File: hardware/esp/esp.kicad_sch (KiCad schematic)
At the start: 41 parts, among them J1 Conn_01x02, J2 USB_C_Receptacle_USB2.0_16P, J3 USB_C_Receptacle_USB2.0_16P, J4 Conn_01x02, SW1 RESET, SW2 BOOT, U1 AMS1117-3.3, U2 CP2102N-Axx-xQFN20, U3 ESP32-S3-WROOM-1

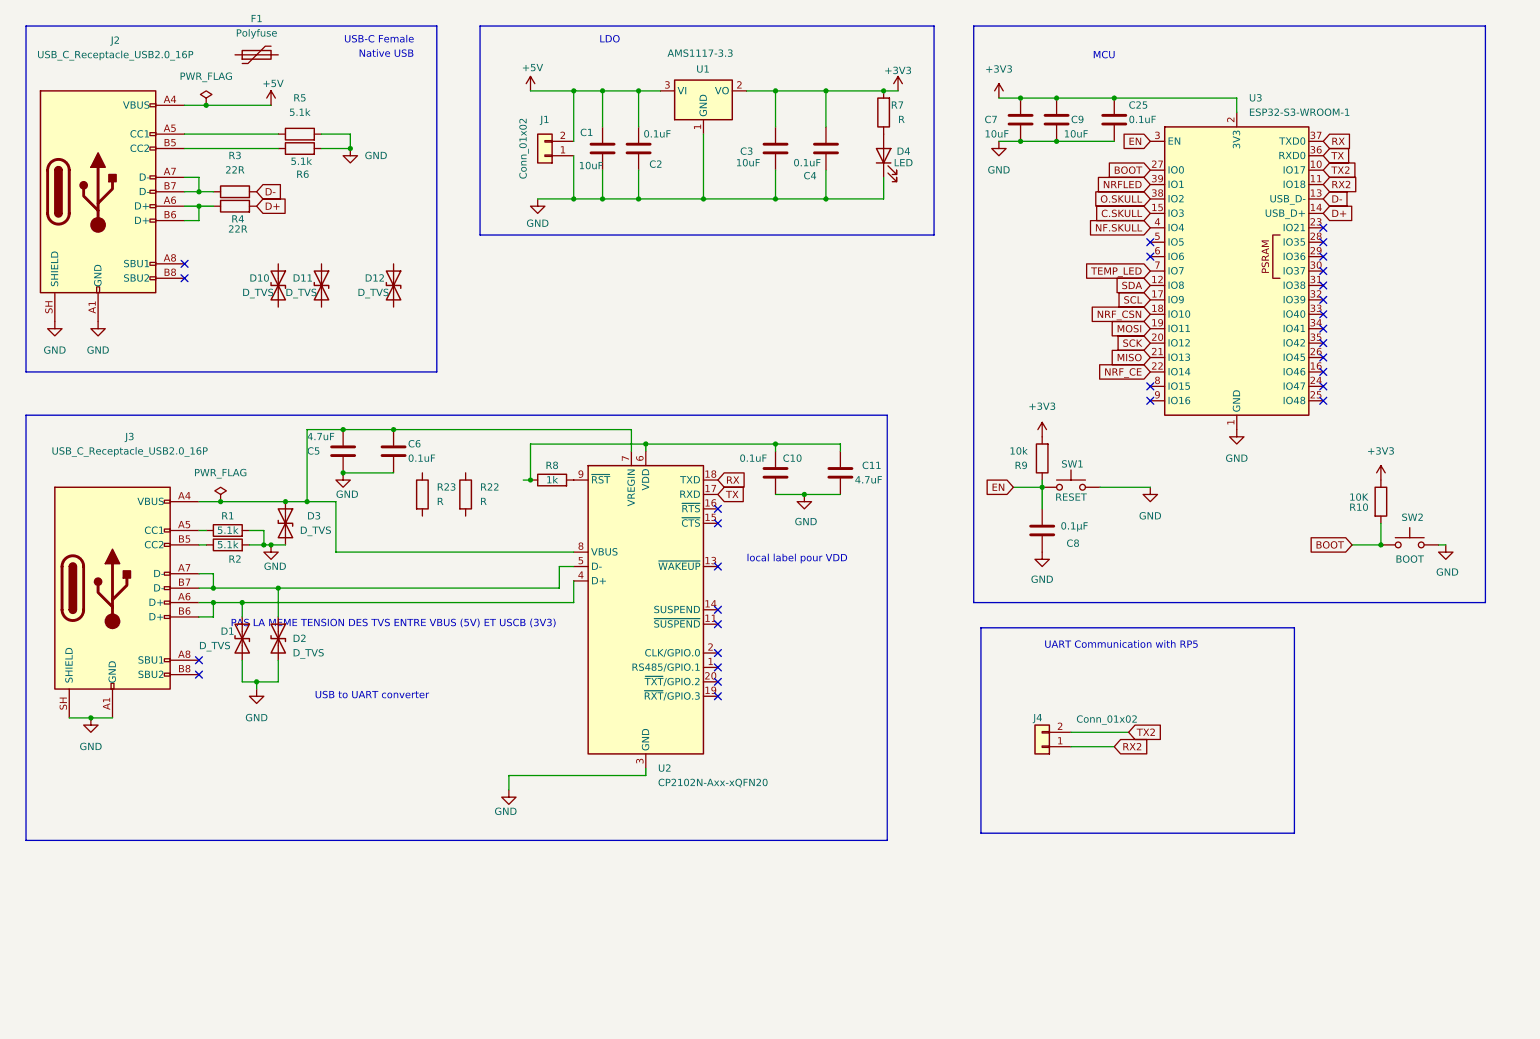
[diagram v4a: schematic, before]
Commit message: Updating schemaitc, and component placement on PCB
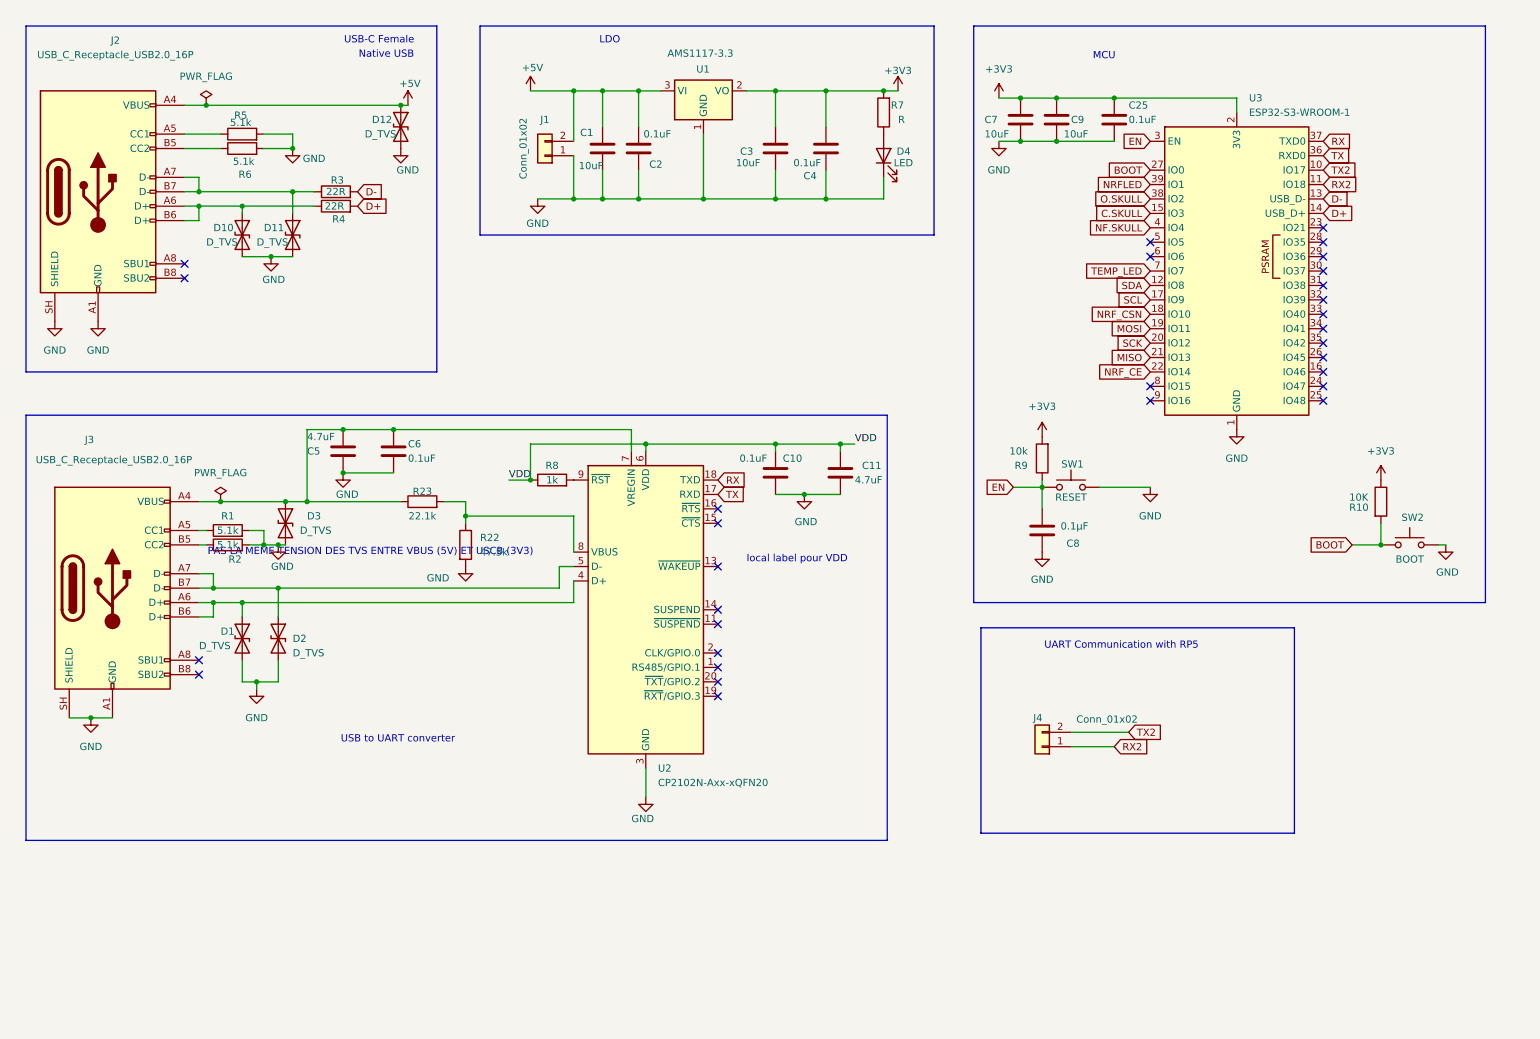
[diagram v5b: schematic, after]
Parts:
- removed F1: Polyfuse, symbol Device:Polyfuse
- R22: value R -> 47.5k; footprint (none) -> Resistor_SMD:R_0805_2012Metric
- R23: value R -> 22.1k; footprint (none) -> Resistor_SMD:R_0805_2012Metric
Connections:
- net +5V: now also D12.1 (A1)
- net GND: now also D10.2 (A2), D11.2 (A2), D12.2 (A2), R22.2
- net at D11.1 (A1): now also J2.A7 (D-), J2.B7 (D-), R3.1
- net VDD: now reaches C10.1, C11.1, R8.1, U2.6 (VDD)
- net at R22.1: now also R23.2, U2.8 (VBUS)
- net at C5.1, C6.1, D3.1 (A1)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: now also R23.1; no longer U2.8 (VBUS)
- net at J2.A6 (D+), J2.B6 (D+), R4.1: now also D10.1 (A1)
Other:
- moved on the sheet: D10, D11, D12, R22, R23, R3, R4, R5, R6

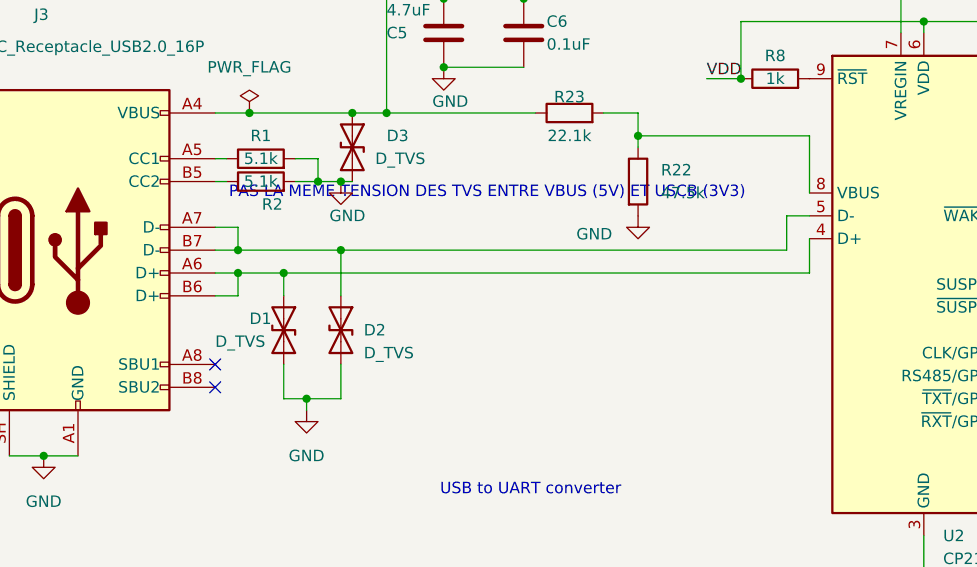
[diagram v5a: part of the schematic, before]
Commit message: Updating schematic, BOM, and component placement on PCB
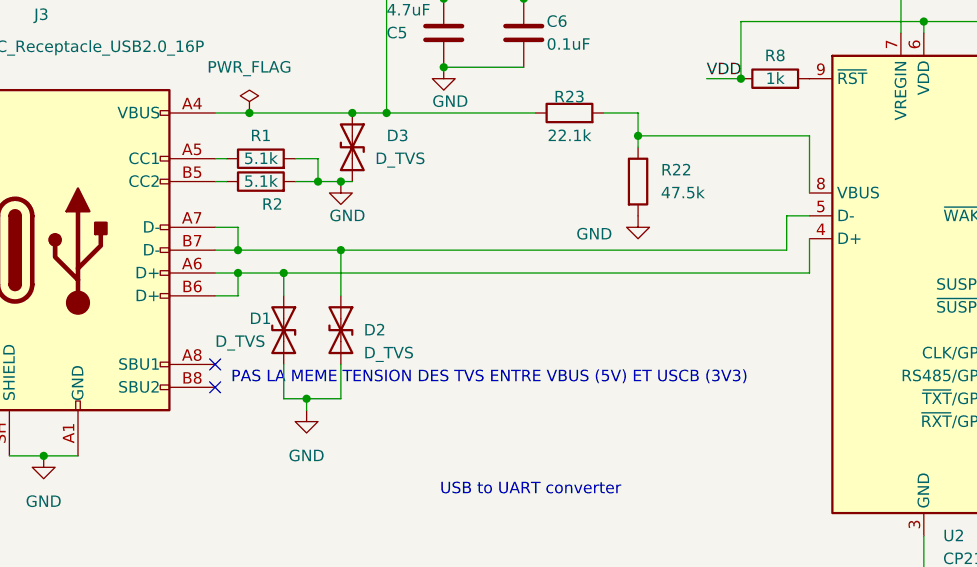
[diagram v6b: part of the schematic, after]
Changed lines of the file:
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@@
 	(text "PAS LA MEME TENSION DES TVS ENTRE VBUS (5V) ET USCB (3V3)"
 		(exclude_from_sim no)
-		(at 79.756 107.95 0)
+		(at 80.01 128.524 0)
 		(effects
 			(font

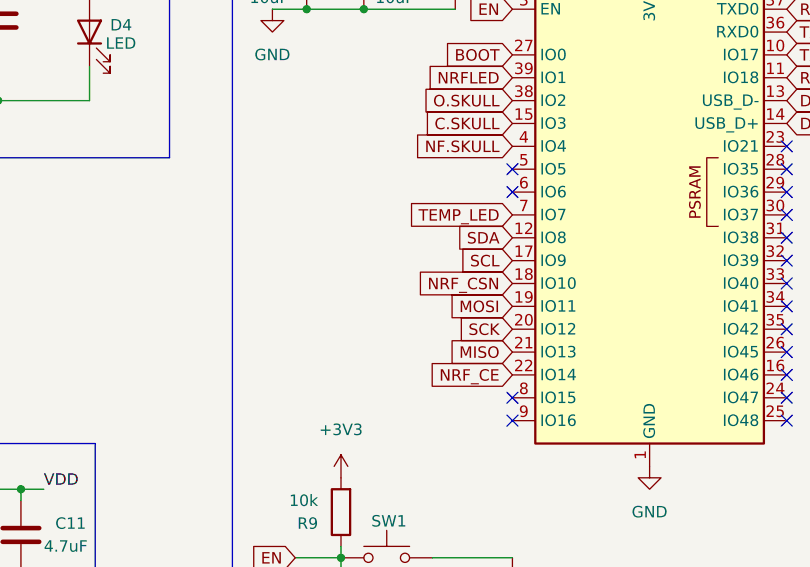
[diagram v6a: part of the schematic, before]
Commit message: Starting PCB routing, updating schematic pins and firmware pins for optimal routing
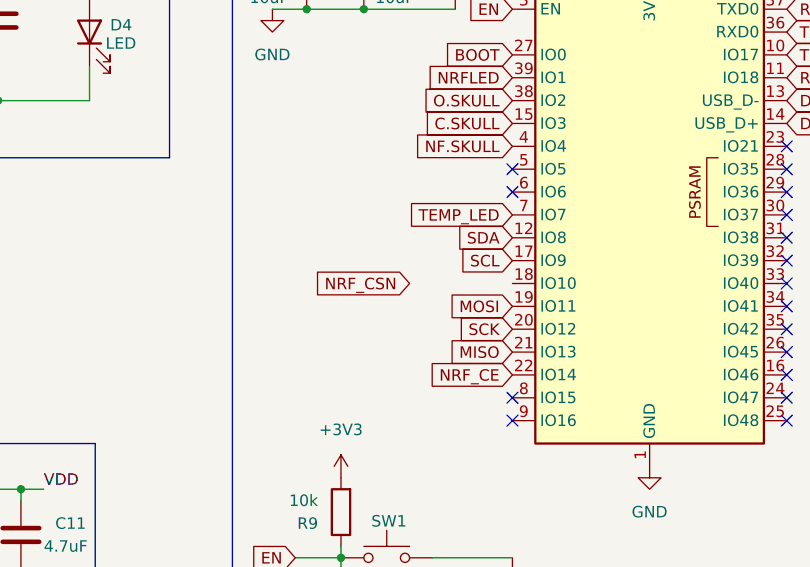
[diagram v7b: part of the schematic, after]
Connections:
- net NRF_CSN: no longer U3.18 (IO10)
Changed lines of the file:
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@@
 	(global_label "NRF_CSN"
 		(shape input)
-		(at 217.17 66.04 180)
+		(at 205.74 66.04 180)
 		(fields_autoplaced yes)
 		(effects
@@
 		)
 		(property "Intersheetrefs" "${INTERSHEET_REFS}"
-			(at 204.9319 66.04 0)
+			(at 193.5019 66.04 0)
 			(hide yes)
 			(show_name no)

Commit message: Finishing PCB routing (PRE-DRC)
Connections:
- net +5V: now also C5.1, C6.1, D3.1 (A1), J3.A4 (VBUS), J3.A9 (VBUS), J3.B4 (VBUS), J3.B9 (VBUS), R23.1, U2.7 (VREGIN)
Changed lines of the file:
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@@
+	)
+	(junction
+		(at 125.73 86.36)
+		(diameter 0)
+		(color 0 0 0 0)
 	)
 	(junction
@@
 					(unit 1)
 				)
+			)
+		)
+	)
+	(symbol
+		(lib_id "power:+5V")
+		(at 125.73 86.36 0)
+		(unit 1)
+		(body_style 1)
+		(exclude_from_sim no)
+		(in_bom yes)
+		(on_board yes)
+		(in_pos_files yes)
+		(dnp no)
+		(property "Reference" "#PWR058"
+			(at 125.73 90.17 0)
+			(hide yes)
+			(show_name no)
+			(do_not_autoplace no)
+			(effects
+				(font
+					(size 1.27 1.27)
+				)
+			)
+		)
+		(property "Value" "+5V"
+			(at 124.206 82.55 0)
+			(show_name no)
+			(do_not_autoplace no)
+			(effects
+				(font
+					(size 1.27 1.27)
+				)
+				(justify left)
+			)
+		)
+		(property "Footprint" ""
+			(at 125.73 86.36 0)
+			(hide yes)
+			(show_name no)
+			(do_not_autoplace no)
+			(effects
+				(font
+					(size 1.27 1.27)
+				)
+			)
+		)
+		(property "Datasheet" ""
+			(at 125.73 86.36 0)
+			(hide yes)
+			(show_name no)
+			(do_not_autoplace no)
+			(effects
+				(font
+					(size 1.27 1.27)
+				)
+			)
+		)
+		(property "Description" "Power symbol creates a global label with name \"+5V\""
+			(at 125.73 86.36 0)
+			(hide yes)
+			(show_name no)
+			(do_not_autoplace no)
+			(effects
+				(font
+					(size 1.27 1.27)
+				)
+			)
+		)
+		(pin "1"
+		)
+		(instances
+			(project "esp"
+				(path "/1af9f8de-01c4-4db4-9e1a-5a2acf839c86"
+					(reference "#PWR058")
+					(unit 1)
+				)
